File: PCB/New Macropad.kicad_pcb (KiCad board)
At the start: 2 copper layers, 64.3 x 70.1 mm, 15 parts, among them J1 Conn_01x04_Pin, SW1 SW_Push, SW2 SW_Push, SW3 SW_Push, SW4 SW_Push, SW5 SW_Push, SW6 SW_Push, U1 XIAO-RP2040-DIP

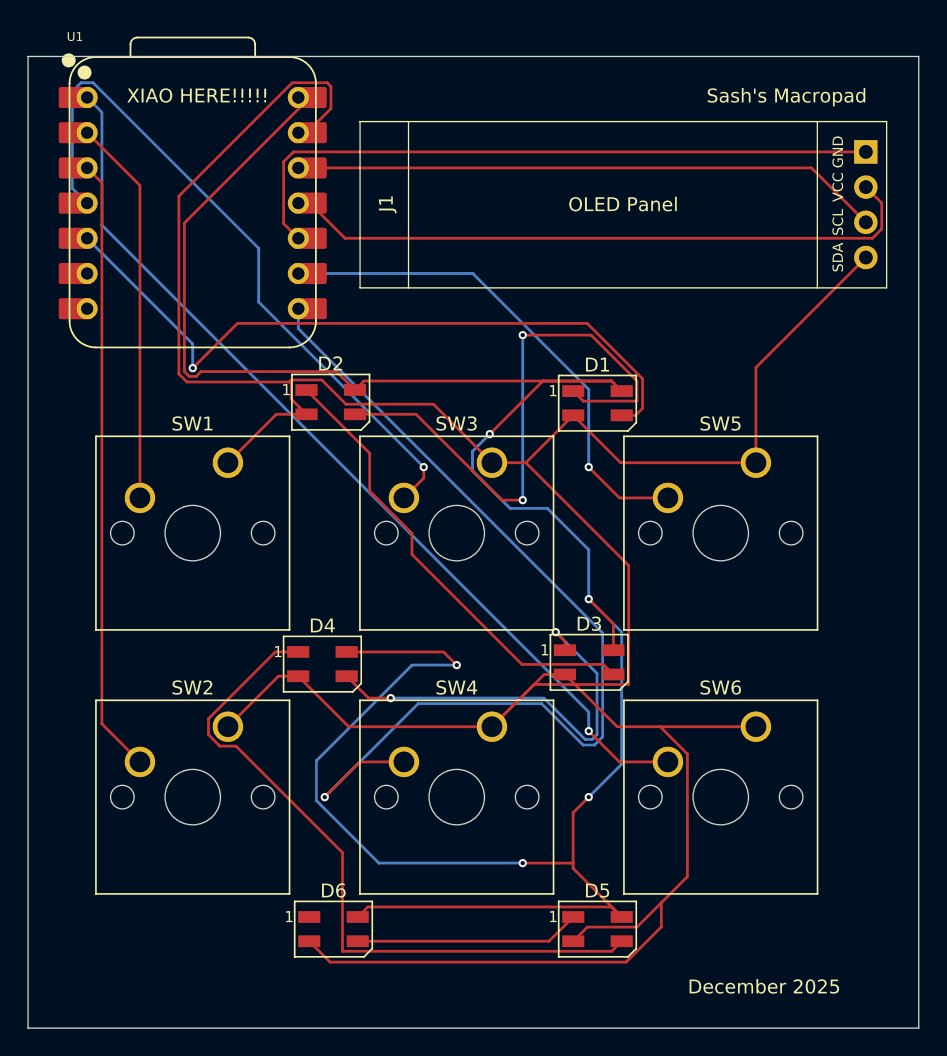
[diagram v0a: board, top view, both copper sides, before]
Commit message: Changed PCB OLED wiring
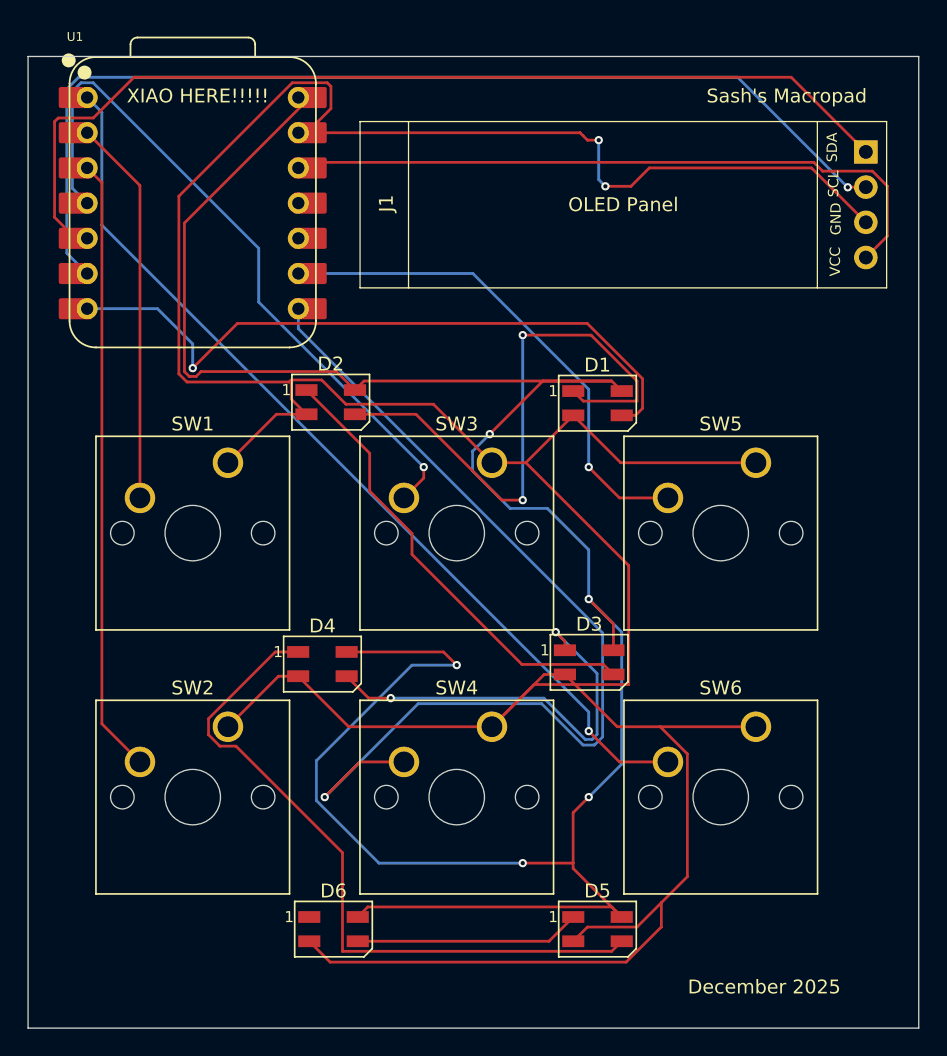
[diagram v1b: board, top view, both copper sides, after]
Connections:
- J1 pad 3: Net-(J1-Pin_3) -> GND
- J1 pad 4: GND -> Net-(J1-Pin_4)
- U1 pad 10: Net-(J1-Pin_1) -> unconnected-(U1-GPIO4/MISO-Pad10)
- U1 pad 11: Net-(J1-Pin_2) -> unconnected-(U1-GPIO3/MOSI-Pad11)
- U1 pad 12: Net-(J1-Pin_3) -> Net-(J1-Pin_4)
- U1 pad 5: Net-(D1-DIN) -> Net-(J1-Pin_1)
- U1 pad 6: unconnected-(U1-GPIO7/SCL-Pad6) -> Net-(J1-Pin_2)
- U1 pad 7: unconnected-(U1-GPIO0/TX-Pad7) -> Net-(D1-DIN)
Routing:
- net Net-(J1-Pin_4): track 0.00 -> 48.4 mm
- net Net-(J1-Pin_3): track 41.7 -> 0.00 mm
- net Net-(J1-Pin_2): track 46.1 -> 75.2 mm, vias 0 -> 1
- net GND: track 232.4 -> 259.9 mm, vias 0 -> 2
- net Net-(J1-Pin_1): track 48.3 -> 71.2 mm
- net Net-(D1-DIN): track 51.8 -> 49.7 mm
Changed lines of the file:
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@@
 	(net 8 "Net-(D5-DOUT)")
 	(net 9 "unconnected-(D6-DOUT-Pad1)")
-	(net 10 "Net-(J1-Pin_3)")
+	(net 10 "Net-(J1-Pin_4)")
 	(net 11 "Net-(J1-Pin_1)")
 	(net 12 "Net-(J1-Pin_2)")
@@
 	(net 17 "Net-(U1-GPIO2{slash}SCK)")
 	(net 18 "Net-(U1-GPIO26{slash}ADC0{slash}A0)")
-	(net 19 "unconnected-(U1-GPIO0{slash}TX-Pad7)")
-	(net 20 "unconnected-(U1-GPIO7{slash}SCL-Pad6)")
+	(net 19 "unconnected-(U1-GPIO4{slash}MISO-Pad10)")
+	(net 20 "unconnected-(U1-GPIO3{slash}MOSI-Pad11)")
 	(footprint "LED_SMD:LED_SK6812MINI_PLCC4_3.5x3.5mm_P1.75mm"
 		(layer "F.Cu")
@@
 			(layers "F.Cu" "F.Mask")
 			(roundrect_rratio 0.1)
-			(net 1 "Net-(D1-DIN)")
+			(net 11 "Net-(J1-Pin_1)")
 			(pinfunction "GPIO6/SDA")
 			(pintype "passive")
@@
 			(layers "*.Cu" "*.Mask")
 			(remove_unused_layers no)
-			(net 1 "Net-(D1-DIN)")
+			(net 11 "Net-(J1-Pin_1)")
 			(pinfunction "GPIO6/SDA")
 			(pintype "passive")
@@
 			(layers "F.Cu" "F.Mask")
 			(roundrect_rratio 0.1)
-			(net 20 "unconnected-(U1-GPIO7{slash}SCL-Pad6)")
+			(net 12 "Net-(J1-Pin_2)")
 			(pinfunction "GPIO7/SCL")
 			(pintype "passive")
@@
 			(layers "*.Cu" "*.Mask")
 			(remove_unused_layers no)
-			(net 20 "unconnected-(U1-GPIO7{slash}SCL-Pad6)")
+			(net 12 "Net-(J1-Pin_2)")
 			(pinfunction "GPIO7/SCL")
 			(pintype "passive")
@@
 			(layers "F.Cu" "F.Mask")
 			(roundrect_rratio 0.1)
-			(net 19 "unconnected-(U1-GPIO0{slash}TX-Pad7)")
+			(net 1 "Net-(D1-DIN)")
 			(pinfunction "GPIO0/TX")
 			(pintype "passive")
@@
 			(layers "*.Cu" "*.Mask")
 			(remove_unused_layers no)
-			(net 19 "unconnected-(U1-GPIO0{slash}TX-Pad7)")
+			(net 1 "Net-(D1-DIN)")
 			(pinfunction "GPIO0/TX")
 			(pintype "passive")
@@
 			(layers "*.Cu" "*.Mask")
 			(remove_unused_layers no)
-			(net 11 "Net-(J1-Pin_1)")
+			(net 19 "unconnected-(U1-GPIO4{slash}MISO-Pad10)")
 			(pinfunction "GPIO4/MISO")
 			(pintype "passive")
@@
 			(layers "F.Cu" "F.Mask")
 			(roundrect_rratio 0.1)
-			(net 11 "Net-(J1-Pin_1)")
+			(net 19 "unconnected-(U1-GPIO4{slash}MISO-Pad10)")
 			(pinfunction "GPIO4/MISO")
 			(pintype "passive")
@@
 			(layers "*.Cu" "*.Mask")
 			(remove_unused_layers no)
-			(net 12 "Net-(J1-Pin_2)")
+			(net 20 "unconnected-(U1-GPIO3{slash}MOSI-Pad11)")
 			(pinfunction "GPIO3/MOSI")
 			(pintype "passive")
@@
 			(layers "F.Cu" "F.Mask")
 			(roundrect_rratio 0.1)
-			(net 12 "Net-(J1-Pin_2)")
+			(net 20 "unconnected-(U1-GPIO3{slash}MOSI-Pad11)")
 			(pinfunction "GPIO3/MOSI")
 			(pintype "passive")
@@
 			(layers "*.Cu" "*.Mask")
 			(remove_unused_layers no)
-			(net 10 "Net-(J1-Pin_3)")
+			(net 10 "Net-(J1-Pin_4)")
 			(pinfunction "3V3")
 			(pintype "passive")
@@
 			(layers "F.Cu" "F.Mask")
 			(roundrect_rratio 0.1)
-			(net 10 "Net-(J1-Pin_3)")
+			(net 10 "Net-(J1-Pin_4)")
 			(pinfunction "3V3")
 			(pintype "passive")
@@
 		)
 		(fp_text user "GND"
-			(at 34.5 2.19 270)
+			(at 34.335 7.0225 270)
 			(layer "F.SilkS")
 			(effects
@@
 		)
 		(fp_text user "VCC"
-			(at 34.5 4.73 270)
+			(at 34.285 10.1025 270)
 			(layer "F.SilkS")
 			(effects
@@
 		)
 		(fp_text user "SDA"
-			(at 34.5 9.81 270)
+			(at 34.065 1.8625 270)
 			(layer "F.SilkS")
 			(effects
@@
 		)
 		(fp_text user "SCL"
-			(at 34.5 7.27 270)
+			(at 34.165 4.4925 270)
 			(layer "F.SilkS")
 			(effects
@@
 			(layers "*.Cu" "*.Mask")
 			(remove_unused_layers no)
-			(net 10 "Net-(J1-Pin_3)")
+			(net 3 "GND")
 			(pinfunction "Pin_3")
 			(pintype "passive")
@@
 			(layers "*.Cu" "*.Mask")
 			(remove_unused_layers no)
-			(net 3 "GND")
+			(net 10 "Net-(J1-Pin_4)")
 			(pinfunction "Pin_4")
 			(pintype "passive")
@@
 	)
 	(segment
+		(start 137.95375 50.4825)
+		(end 132.87375 50.4825)
+		(width 0.2)
+		(layer "B.Cu")
+		(net 1)
+	)
+	(segment
 		(start 140.49375 53.0225)
-		(end 132.87375 45.4025)
+		(end 137.95375 50.4825)
 		(width 0.2)
 		(layer "B.Cu")
@@
 	)
 	(segment
+		(start 168.98 38.32)
+		(end 169.79 38.32)
+		(width 0.2)
+		(layer "F.Cu")
+		(net 3)
+	)
+	(segment
 		(start 146.67875 77)
 		(end 148.1 77)
@@
 	)
 	(segment
+		(start 168.4425 37.7825)
+		(end 168.66 38)
+		(width 0.2)
+		(layer "F.Cu")
+		(net 3)
+	)
+	(segment
 		(start 172.551 95.101)
 		(end 174.30725 93.34475)
@@
 	)
 	(segment
-		(start 181.13375 54.71875)
-		(end 189.065 46.7875)
-		(width 0.2)
-		(layer "F.Cu")
-		(net 3)
-	)
-	(segment
 		(start 147.599 55.624)
 		(end 149.801 55.624)
@@
 	)
 	(segment
+		(start 168.66 38)
+		(end 168.98 38.32)
+		(width 0.2)
+		(layer "F.Cu")
+		(net 3)
+	)
+	(segment
 		(start 165.85375 76.875)
 		(end 167.35 76.875)
@@
 	)
 	(segment
+		(start 148.94875 37.7825)
+		(end 168.4425 37.7825)
+		(width 0.2)
+		(layer "F.Cu")
+		(net 3)
+	)
+	(segment
 		(start 147.67344 34.1795)
 		(end 139.49175 42.36119)
@@
 	)
 	(segment
+		(start 189.065 44.2475)
+		(end 185.14 40.3225)
+		(width 0.2)
+		(layer "F.Cu")
+		(net 3)
+	)
+	(segment
 		(start 148.11375 37.7825)
 		(end 148.727376 37.7825)
@@
 	)
 	(segment
+		(start 170.27 41.65)
+		(end 172.1125 41.65)
+		(width 0.2)
+		(layer "F.Cu")
+		(net 3)
+	)
+	(segment
 		(start 149.801 55.624)
 		(end 151.551 57.374)
@@
 	)
 	(segment
-		(start 181.13375 61.595)
-		(end 181.13375 54.71875)
+		(start 185.14 40.3225)
+		(end 173.44 40.3225)
 		(width 0.2)
 		(layer "F.Cu")
@@
 	)
 	(segment
+		(start 172.1125 41.65)
+		(end 173.44 40.3225)
+		(width 0.2)
+		(layer "F.Cu")
+		(net 3)
+	)
+	(segment
 		(start 174.30725 95.09475)
 		(end 174.30725 93.34475)
@@
 		(net 3)
 	)
+	(via
+		(at 170.27 41.65)
+		(size 0.6)
+		(drill 0.3)
+		(layers "F.Cu" "B.Cu")
+		(net 3)
+	)
+	(via
+		(at 169.79 38.32)
+		(size 0.6)
+		(drill 0.3)
+		(layers "F.Cu" "B.Cu")
+		(net 3)
+	)
+	(segment
+		(start 169.79 41.17)
+		(end 170.27 41.65)
+		(width 0.2)
+		(layer "B.Cu")
+		(net 3)
+	)
+	(segment
+		(start 169.79 38.32)
+		(end 169.79 41.17)
+		(width 0.2)
+		(layer "B.Cu")
+		(net 3)
+	)
 	(segment
 		(start 172.551 57.151)
@@
 	)
 	(segment
-		(start 185.14 40.3225)
-		(end 148.94875 40.3225)
+		(start 190.617 41.63174)
+		(end 189.54176 40.5565)
 		(width 0.2)
 		(layer "F.Cu")
@@
 	)
 	(segment
-		(start 189.065 44.2475)
-		(end 185.14 40.3225)
+		(start 190.617 45.2355)
+		(end 190.617 41.63174)
+		(width 0.2)
+		(layer "F.Cu")
+		(net 10)
+	)
+	(segment
+		(start 185.9411 40.5565)
+		(end 185.3061 39.9215)
+		(width 0.2)
+		(layer "F.Cu")
+		(net 10)
+	)
+	(segment
+		(start 185.3061 39.9215)
+		(end 148.94875 39.9215)
 		(width 0.2)
 		(layer "F.Cu")
@@
 	)
 	(segment
-		(start 147.76544 39.1675)
-		(end 147.05075 39.88219)
+		(start 189.065 46.7875)
+		(end 189.0675 46.79)
+		(width 0.2)
+		(layer "F.Cu")
+		(net 10)
+	)
+	(segment
+		(start 189.065 46.7875)
+		(end 190.617 45.2355)
+		(width 0.2)
+		(layer "F.Cu")
+		(net 10)
+	)
+	(segment
+		(start 189.0675 46.79)
+		(end 189.25 46.79)
+		(width 0.2)
+		(layer "F.Cu")
+		(net 10)
+	)
+	(segment
+		(start 189.54176 40.5565)
+		(end 185.9411 40.5565)
+		(width 0.2)
+		(layer "F.Cu")
+		(net 10)
+	)
+	(segment
+		(start 130.783124 36.7195)
+		(end 130.52175 36.980874)
 		(width 0.2)
 		(layer "F.Cu")
@@
 	)
 	(segment
-		(start 147.05075 39.88219)
-		(end 147.05075 44.3395)
+		(start 136.25506 33.7785)
+		(end 133.31406 36.7195)
 		(width 0.2)
 		(layer "F.Cu")
@@
 	)
 	(segment
-		(start 147.05075 44.3395)
-		(end 148.11375 45.4025)
+		(start 133.31406 36.7195)
+		(end 130.783124 36.7195)
 		(width 0.2)
 		(layer "F.Cu")
@@
 	(segment
 		(start 189.065 39.1675)
-		(end 147.76544 39.1675)
+		(end 183.676 33.7785)
+		(width 0.2)
+		(layer "F.Cu")
+		(net 11)
+	)
+	(segment
+		(start 183.676 33.7785)
+		(end 136.25506 33.7785)
 		(width 0.2)
 		(layer "F.Cu")
@@
 	)
 	(segment
-		(start 151.48475 45.3985)
-		(end 148.94875 42.8625)
+		(start 130.52175 36.980874)
+		(end 130.52175 43.8855)
+		(width 0.2)
+		(layer "F.Cu")
+		(net 11)
+	)
+	(segment
+		(start 130.52175 43.8855)
+		(end 132.03875 45.4025)
+		(width 0.2)
+		(layer "F.Cu")
+		(net 11)
+	)
+	(segment
+		(start 187.7725 41.7075)
+		(end 187.76 41.72)
 		(width 0.2)
 		(layer "F.Cu")
@@
 	(segment
 		(start 189.065 41.7075)
-		(end 190.216 42.8585)
+		(end 187.7725 41.7075)
 		(width 0.2)
 		(layer "F.Cu")
 		(net 12)
 	)
+	(via
+		(at 187.76 41.72)
+		(size 0.6)
+		(drill 0.3)
+		(layers "F.Cu" "B.Cu")
+		(net 12)
+	)
 	(segment
-		(start 189.54176 45.3985)
-		(end 151.48475 45.3985)
+		(start 132.26734 33.7785)
+		(end 131.40975 34.63609)
 		(width 0.2)
-		(layer "F.Cu")
+		(layer "B.Cu")
 		(net 12)
 	)
 	(segment
-		(start 190.216 42.8585)
-		(end 190.216 44.72426)
+		(start 131.40975 46.4785)
+		(end 132.87375 47.9425)
 		(width 0.2)
-		(layer "F.Cu")
+		(layer "B.Cu")
 		(net 12)
 	)
 	(segment
-		(start 190.216 44.72426)
-		(end 189.54176 45.3985)
+		(start 179.8185 33.7785)
+		(end 132.26734 33.7785)
 		(width 0.2)
-		(layer "F.Cu")
+		(layer "B.Cu")
+		(net 12)
+	)
+	(segment
+		(start 131.40975 34.63609)
+		(end 131.40975 46.4785)
+		(width 0.2)
+		(layer "B.Cu")
+		(net 12)
+	)
+	(segment
+		(start 187.76 41.72)
+		(end 179.8185 33.7785)
+		(width 0.2)
+		(layer "B.Cu")
 		(net 12)
 	)
